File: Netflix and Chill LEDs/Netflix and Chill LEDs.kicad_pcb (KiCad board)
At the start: 2 copper layers, 17.8 x 48.3 mm, 0 parts

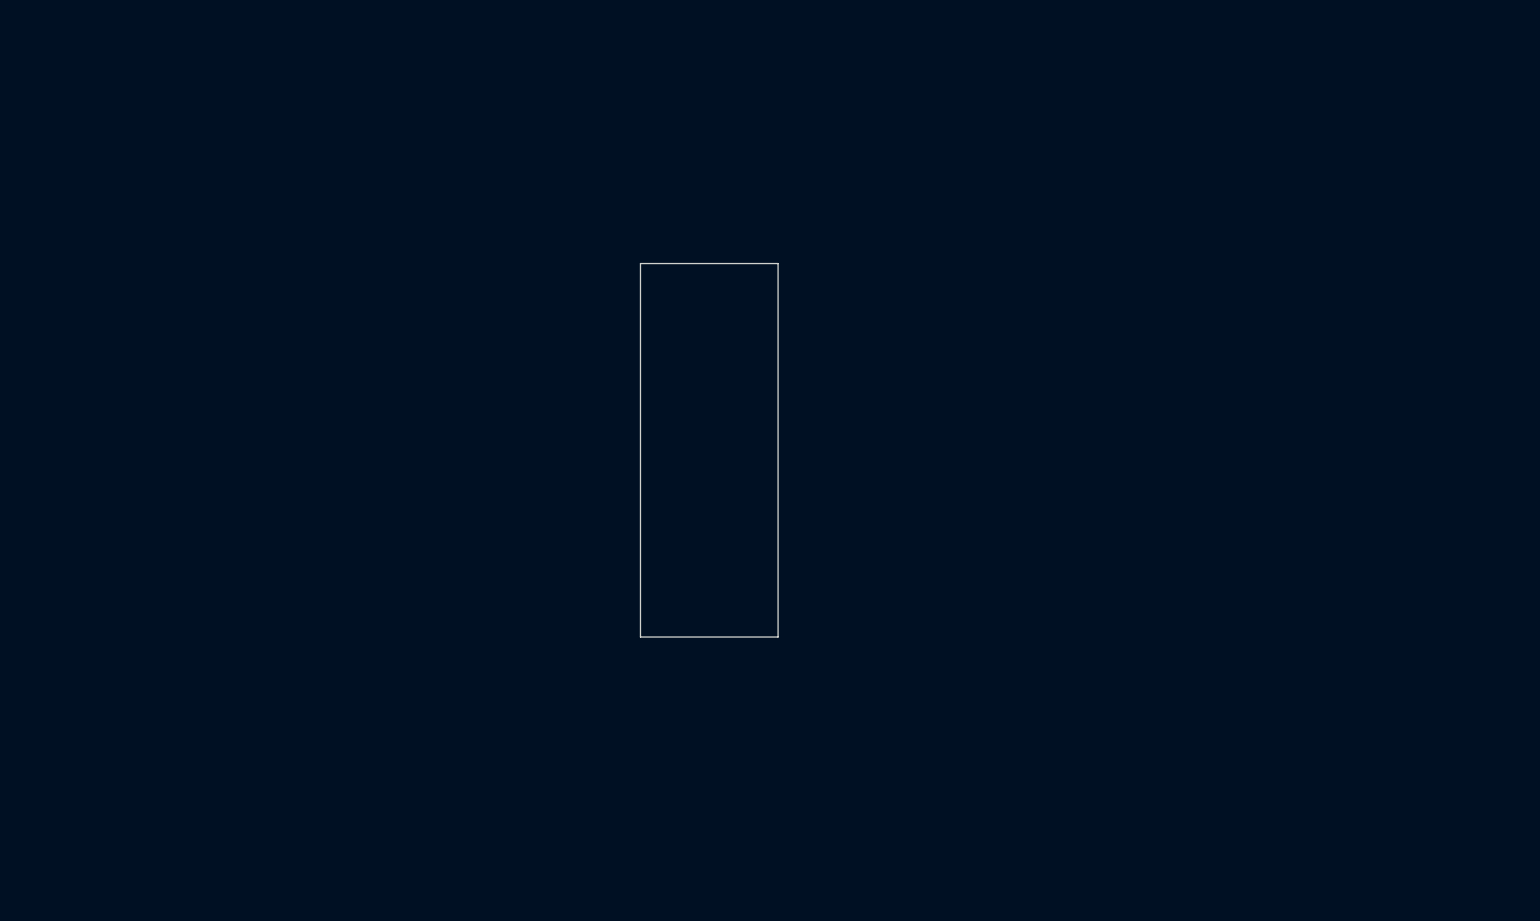
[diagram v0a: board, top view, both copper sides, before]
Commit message: board base design done
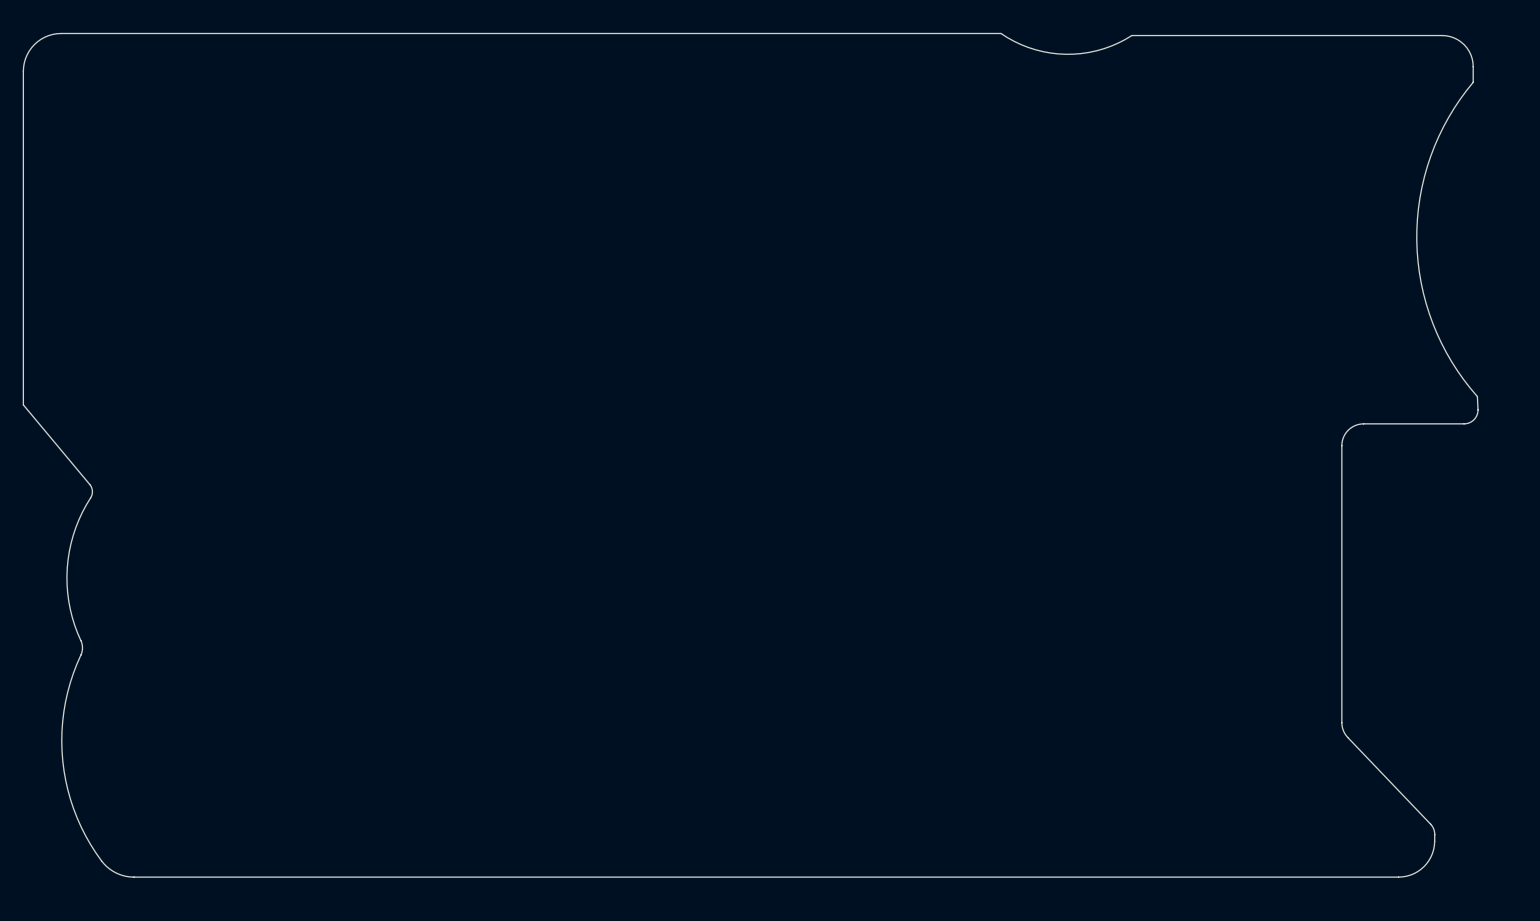
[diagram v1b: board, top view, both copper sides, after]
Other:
- board size 17.8 x 48.3 mm -> 188 x 109 mm

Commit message: placement and routing done
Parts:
- added C1: 1uF, Capacitor_SMD:C_0603_1608Metric, F.Cu at (62.0, 38.8)
- added C10: 1uF, Capacitor_SMD:C_0603_1608Metric, F.Cu at (206.8, 38.8)
- added C11: 1uF, Capacitor_SMD:C_0603_1608Metric, F.Cu at (223.0, 38.8)
- added C12: 1uF, Capacitor_SMD:C_0603_1608Metric, F.Cu at (238.8, 38.8)
- added C13: 1uF, Capacitor_SMD:C_0603_1608Metric, F.Cu at (60.5, 58.8)
- added C14: 1uF, Capacitor_SMD:C_0603_1608Metric, F.Cu at (78.0, 58.8)
- added C15: 1uF, Capacitor_SMD:C_0603_1608Metric, F.Cu at (94.5, 58.8)
- added C16: 1uF, Capacitor_SMD:C_0603_1608Metric, F.Cu at (105.2, 58.8)
- added C17: 1uF, Capacitor_SMD:C_0603_1608Metric, F.Cu at (129.0, 58.8)
- added C18: 1uF, Capacitor_SMD:C_0603_1608Metric, F.Cu at (151.8, 58.8)
- added C19: 1uF, Capacitor_SMD:C_0603_1608Metric, F.Cu at (162.0, 58.8)
- added C2: 1uF, Capacitor_SMD:C_0603_1608Metric, F.Cu at (78.0, 38.8)
- added C20: 1uF, Capacitor_SMD:C_0603_1608Metric, F.Cu at (179.5, 58.8)
- added C21: 1uF, Capacitor_SMD:C_0603_1608Metric, F.Cu at (206.8, 58.8)
- added C22: 1uF, Capacitor_SMD:C_0603_1608Metric, F.Cu at (231.0, 58.8)
- added C23: 1uF, Capacitor_SMD:C_0603_1608Metric, F.Cu at (60.5, 80.2)
- added C24: 1uF, Capacitor_SMD:C_0603_1608Metric, F.Cu at (77.0, 80.2)
- added C25: 1uF, Capacitor_SMD:C_0603_1608Metric, F.Cu at (94.5, 80.2)
- added C26: 1uF, Capacitor_SMD:C_0603_1608Metric, F.Cu at (107.0, 80.2)
- added C27: 1uF, Capacitor_SMD:C_0603_1608Metric, F.Cu at (129.0, 80.2)
- added C28: 1uF, Capacitor_SMD:C_0603_1608Metric, F.Cu at (151.8, 80.2)
- added C29: 1uF, Capacitor_SMD:C_0603_1608Metric, F.Cu at (179.5, 80.2)
- added C3: 1uF, Capacitor_SMD:C_0603_1608Metric, F.Cu at (94.5, 38.8)
- added C30: 1uF, Capacitor_SMD:C_0603_1608Metric, F.Cu at (192.0, 80.2)
- added C31: 1uF, Capacitor_SMD:C_0603_1608Metric, F.Cu at (206.8, 80.2)
- added C32: 1uF, Capacitor_SMD:C_0603_1608Metric, F.Cu at (222.5, 80.2)
- added C33: 1uF, Capacitor_SMD:C_0603_1608Metric, F.Cu at (238.8, 80.2)
- added C34: 1uF, Capacitor_SMD:C_0603_1608Metric, F.Cu at (79.8, 96.2)
- added C35: 1uF, Capacitor_SMD:C_0603_1608Metric, F.Cu at (117.8, 96.2)
- added C36: 1uF, Capacitor_SMD:C_0603_1608Metric, F.Cu at (144.8, 96.2)
- added C37: 1uF, Capacitor_SMD:C_0603_1608Metric, F.Cu at (160.2, 96.2)
- added C38: 1uF, Capacitor_SMD:C_0603_1608Metric, F.Cu at (177.2, 96.2)
- added C39: 1uF, Capacitor_SMD:C_0603_1608Metric, F.Cu at (194.0, 96.2)
- added C4: 1uF, Capacitor_SMD:C_0603_1608Metric, F.Cu at (107.0, 38.8)
- added C40: 1uF, Capacitor_SMD:C_0603_1608Metric, F.Cu at (221.8, 96.2)
- added C41: 1uF, Capacitor_SMD:C_0603_1608Metric, F.Cu at (67.2, 103.0)
- added C42: 1uF, Capacitor_SMD:C_0603_1608Metric, F.Cu at (129.2, 104.8)
- added C43: 1uF, Capacitor_SMD:C_0603_1608Metric, F.Cu at (71.5, 115.8)
- added C44: 1uF, Capacitor_SMD:C_0603_1608Metric, F.Cu at (82.8, 115.8)
- added C45: 1uF, Capacitor_SMD:C_0603_1608Metric, F.Cu at (114.2, 115.8)
- added C46: 1uF, Capacitor_SMD:C_0603_1608Metric, F.Cu at (144.8, 115.8)
- added C47: 1uF, Capacitor_SMD:C_0603_1608Metric, F.Cu at (160.2, 115.8)
- added C48: 1uF, Capacitor_SMD:C_0603_1608Metric, F.Cu at (177.2, 115.8)
- added C49: 1uF, Capacitor_SMD:C_0603_1608Metric, F.Cu at (194.0, 115.8)
- added C5: 1uF, Capacitor_SMD:C_0603_1608Metric, F.Cu at (121.0, 38.8)
- added C50: 1uF, Capacitor_SMD:C_0603_1608Metric, F.Cu at (221.8, 115.8)
- added C51: 1uF, Capacitor_SMD:C_0603_1608Metric, F.Cu at (129.2, 127.2)
- added C52: 1uF, Capacitor_SMD:C_0603_1608Metric, F.Cu at (67.2, 131.8)
- added C53: 1uF, Capacitor_SMD:C_0603_1608Metric, F.Cu at (82.2, 137.8)
- added C54: 1uF, Capacitor_SMD:C_0603_1608Metric, F.Cu at (117.2, 137.8)
- added C55: 1uF, Capacitor_SMD:C_0603_1608Metric, F.Cu at (144.8, 137.8)
- added C56: 1uF, Capacitor_SMD:C_0603_1608Metric, F.Cu at (160.2, 137.8)
- added C57: 1uF, Capacitor_SMD:C_0603_1608Metric, F.Cu at (177.2, 137.8)
- added C58: 1uF, Capacitor_SMD:C_0603_1608Metric, F.Cu at (194.0, 137.8)
- added C59: 1uF, Capacitor_SMD:C_0603_1608Metric, F.Cu at (207.0, 137.8)
- added C6: 1uF, Capacitor_SMD:C_0603_1608Metric, F.Cu at (137.2, 38.8)
- added C60: 1uF, Capacitor_SMD:C_0603_1608Metric, F.Cu at (221.8, 137.8)
- added C61: 1uF, Capacitor_SMD:C_0603_1608Metric, F.Cu at (234.0, 137.8)
- added C7: 1uF, Capacitor_SMD:C_0603_1608Metric, F.Cu at (151.8, 38.8)
- added C8: 1uF, Capacitor_SMD:C_0603_1608Metric, F.Cu at (164.5, 38.8)
- added C9: 1uF, Capacitor_SMD:C_0603_1608Metric, F.Cu at (179.5, 38.8)
- added D1: WS2812B, LED_SMD:LED_WS2812B_PLCC4_5.0x5.0mm_P3.2mm, F.Cu at (62.0, 42.5)
- added D10: WS2812B, LED_SMD:LED_WS2812B_PLCC4_5.0x5.0mm_P3.2mm, F.Cu at (206.8, 42.5)
- added D11: WS2812B, LED_SMD:LED_WS2812B_PLCC4_5.0x5.0mm_P3.2mm, F.Cu at (223.0, 42.5)
- added D12: WS2812B, LED_SMD:LED_WS2812B_PLCC4_5.0x5.0mm_P3.2mm, F.Cu at (238.8, 42.5)
- added D13: WS2812B, LED_SMD:LED_WS2812B_PLCC4_5.0x5.0mm_P3.2mm, F.Cu at (60.5, 62.5)
- added D14: WS2812B, LED_SMD:LED_WS2812B_PLCC4_5.0x5.0mm_P3.2mm, F.Cu at (78.0, 62.5)
- added D15: WS2812B, LED_SMD:LED_WS2812B_PLCC4_5.0x5.0mm_P3.2mm, F.Cu at (94.5, 62.5)
- added D16: WS2812B, LED_SMD:LED_WS2812B_PLCC4_5.0x5.0mm_P3.2mm, F.Cu at (105.2, 62.5)
- added D17: WS2812B, LED_SMD:LED_WS2812B_PLCC4_5.0x5.0mm_P3.2mm, F.Cu at (129.0, 62.5)
- added D18: WS2812B, LED_SMD:LED_WS2812B_PLCC4_5.0x5.0mm_P3.2mm, F.Cu at (151.8, 62.5)
- added D19: WS2812B, LED_SMD:LED_WS2812B_PLCC4_5.0x5.0mm_P3.2mm, F.Cu at (162.0, 62.5)
- added D2: WS2812B, LED_SMD:LED_WS2812B_PLCC4_5.0x5.0mm_P3.2mm, F.Cu at (78.0, 42.5)
- added D20: WS2812B, LED_SMD:LED_WS2812B_PLCC4_5.0x5.0mm_P3.2mm, F.Cu at (179.5, 62.5)
- added D21: WS2812B, LED_SMD:LED_WS2812B_PLCC4_5.0x5.0mm_P3.2mm, F.Cu at (206.8, 62.5)
- added D22: WS2812B, LED_SMD:LED_WS2812B_PLCC4_5.0x5.0mm_P3.2mm, F.Cu at (231.0, 62.5)
- added D23: WS2812B, LED_SMD:LED_WS2812B_PLCC4_5.0x5.0mm_P3.2mm, F.Cu at (60.5, 84.0)
- added D24: WS2812B, LED_SMD:LED_WS2812B_PLCC4_5.0x5.0mm_P3.2mm, F.Cu at (77.0, 84.0)
- added D25: WS2812B, LED_SMD:LED_WS2812B_PLCC4_5.0x5.0mm_P3.2mm, F.Cu at (94.5, 84.0)
- added D26: WS2812B, LED_SMD:LED_WS2812B_PLCC4_5.0x5.0mm_P3.2mm, F.Cu at (107.0, 84.0)
- added D27: WS2812B, LED_SMD:LED_WS2812B_PLCC4_5.0x5.0mm_P3.2mm, F.Cu at (129.0, 84.0)
- added D28: WS2812B, LED_SMD:LED_WS2812B_PLCC4_5.0x5.0mm_P3.2mm, F.Cu at (151.8, 84.0)
- added D29: WS2812B, LED_SMD:LED_WS2812B_PLCC4_5.0x5.0mm_P3.2mm, F.Cu at (179.5, 84.0)
- added D3: WS2812B, LED_SMD:LED_WS2812B_PLCC4_5.0x5.0mm_P3.2mm, F.Cu at (94.5, 42.5)
- added D30: WS2812B, LED_SMD:LED_WS2812B_PLCC4_5.0x5.0mm_P3.2mm, F.Cu at (192.0, 84.0)
- added D31: WS2812B, LED_SMD:LED_WS2812B_PLCC4_5.0x5.0mm_P3.2mm, F.Cu at (206.8, 84.0)
- added D32: WS2812B, LED_SMD:LED_WS2812B_PLCC4_5.0x5.0mm_P3.2mm, F.Cu at (222.5, 84.0)
- added D33: WS2812B, LED_SMD:LED_WS2812B_PLCC4_5.0x5.0mm_P3.2mm, F.Cu at (238.8, 84.0)
- added D34: WS2812B, LED_SMD:LED_WS2812B_PLCC4_5.0x5.0mm_P3.2mm, F.Cu at (79.8, 100.0)
- added D35: WS2812B, LED_SMD:LED_WS2812B_PLCC4_5.0x5.0mm_P3.2mm, F.Cu at (117.8, 100.0)
- added D36: WS2812B, LED_SMD:LED_WS2812B_PLCC4_5.0x5.0mm_P3.2mm, F.Cu at (144.8, 100.0)
- added D37: WS2812B, LED_SMD:LED_WS2812B_PLCC4_5.0x5.0mm_P3.2mm, F.Cu at (160.2, 100.0)
- added D38: WS2812B, LED_SMD:LED_WS2812B_PLCC4_5.0x5.0mm_P3.2mm, F.Cu at (177.2, 100.0)
- added D39: WS2812B, LED_SMD:LED_WS2812B_PLCC4_5.0x5.0mm_P3.2mm, F.Cu at (194.0, 100.0)
- added D4: WS2812B, LED_SMD:LED_WS2812B_PLCC4_5.0x5.0mm_P3.2mm, F.Cu at (107.0, 42.5)
- added D40: WS2812B, LED_SMD:LED_WS2812B_PLCC4_5.0x5.0mm_P3.2mm, F.Cu at (221.8, 100.0)
- added D41: WS2812B, LED_SMD:LED_WS2812B_PLCC4_5.0x5.0mm_P3.2mm, F.Cu at (67.2, 106.8)
- added D42: WS2812B, LED_SMD:LED_WS2812B_PLCC4_5.0x5.0mm_P3.2mm, F.Cu at (129.2, 108.5)
- added D43: WS2812B, LED_SMD:LED_WS2812B_PLCC4_5.0x5.0mm_P3.2mm, F.Cu at (71.5, 119.5)
- added D44: WS2812B, LED_SMD:LED_WS2812B_PLCC4_5.0x5.0mm_P3.2mm, F.Cu at (82.8, 119.5)
- added D45: WS2812B, LED_SMD:LED_WS2812B_PLCC4_5.0x5.0mm_P3.2mm, F.Cu at (114.2, 119.5)
- added D46: WS2812B, LED_SMD:LED_WS2812B_PLCC4_5.0x5.0mm_P3.2mm, F.Cu at (144.8, 119.5)
- added D47: WS2812B, LED_SMD:LED_WS2812B_PLCC4_5.0x5.0mm_P3.2mm, F.Cu at (160.2, 119.5)
- added D48: WS2812B, LED_SMD:LED_WS2812B_PLCC4_5.0x5.0mm_P3.2mm, F.Cu at (177.2, 119.5)
- added D49: WS2812B, LED_SMD:LED_WS2812B_PLCC4_5.0x5.0mm_P3.2mm, F.Cu at (194.0, 119.5)
- added D5: WS2812B, LED_SMD:LED_WS2812B_PLCC4_5.0x5.0mm_P3.2mm, F.Cu at (121.0, 42.5)
- added D50: WS2812B, LED_SMD:LED_WS2812B_PLCC4_5.0x5.0mm_P3.2mm, F.Cu at (221.8, 119.5)
- added D51: WS2812B, LED_SMD:LED_WS2812B_PLCC4_5.0x5.0mm_P3.2mm, F.Cu at (129.2, 131.0)
- added D52: WS2812B, LED_SMD:LED_WS2812B_PLCC4_5.0x5.0mm_P3.2mm, F.Cu at (67.2, 135.5)
- added D53: WS2812B, LED_SMD:LED_WS2812B_PLCC4_5.0x5.0mm_P3.2mm, F.Cu at (82.2, 141.5)
- added D54: WS2812B, LED_SMD:LED_WS2812B_PLCC4_5.0x5.0mm_P3.2mm, F.Cu at (117.2, 141.5)
- added D55: WS2812B, LED_SMD:LED_WS2812B_PLCC4_5.0x5.0mm_P3.2mm, F.Cu at (144.8, 141.5)
- added D56: WS2812B, LED_SMD:LED_WS2812B_PLCC4_5.0x5.0mm_P3.2mm, F.Cu at (160.2, 141.5)
- added D57: WS2812B, LED_SMD:LED_WS2812B_PLCC4_5.0x5.0mm_P3.2mm, F.Cu at (177.2, 141.5)
- added D58: WS2812B, LED_SMD:LED_WS2812B_PLCC4_5.0x5.0mm_P3.2mm, F.Cu at (194.0, 141.5)
- added D59: WS2812B, LED_SMD:LED_WS2812B_PLCC4_5.0x5.0mm_P3.2mm, F.Cu at (207.0, 141.5)
- added D6: WS2812B, LED_SMD:LED_WS2812B_PLCC4_5.0x5.0mm_P3.2mm, F.Cu at (137.2, 42.5)
- added D60: WS2812B, LED_SMD:LED_WS2812B_PLCC4_5.0x5.0mm_P3.2mm, F.Cu at (221.8, 141.5)
- added D61: WS2812B, LED_SMD:LED_WS2812B_PLCC4_5.0x5.0mm_P3.2mm, F.Cu at (234.0, 141.5)
- added D7: WS2812B, LED_SMD:LED_WS2812B_PLCC4_5.0x5.0mm_P3.2mm, F.Cu at (151.8, 42.5)
- added D8: WS2812B, LED_SMD:LED_WS2812B_PLCC4_5.0x5.0mm_P3.2mm, F.Cu at (164.5, 42.5)
- added D9: WS2812B, LED_SMD:LED_WS2812B_PLCC4_5.0x5.0mm_P3.2mm, F.Cu at (179.5, 42.5)
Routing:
- net +5V: track 0.00 -> 1328.7 mm
- net Net-(D22-Pad2): track 0.00 -> 189.0 mm
- net Net-(D33-Pad2): track 0.00 -> 177.7 mm
- net GND: track 0.00 -> 172.8 mm, vias 0 -> 122
- net Net-(D40-Pad2): track 0.00 -> 153.4 mm
- net Net-(D50-Pad2): track 0.00 -> 91.0 mm
- net Net-(D42-Pad2): track 0.00 -> 71.6 mm
- net Net-(D41-Pad2): track 0.00 -> 69.1 mm
- net Net-(D51-Pad2): track 0.00 -> 57.6 mm
- net Net-(D34-Pad2): track 0.00 -> 44.2 mm
- net Net-(D53-Pad2): track 0.00 -> 41.2 mm
- net Net-(D44-Pad2): track 0.00 -> 37.7 mm
- net Net-(D45-Pad2): track 0.00 -> 36.7 mm
- net Net-(D39-Pad2): track 0.00 -> 34.0 mm
- net Net-(D49-Pad2): track 0.00 -> 34.0 mm
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- added copper zone on B.Cu, net GND

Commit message: layout done
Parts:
- added J2: CONN_02, Connector_PinHeader_2.54mm:PinHeader_1x02_P2.54mm_Vertical, B.Cu at (218.1, 133.3)
- added U1: PixelBlazePico, _Breadstick_Footprints:PixelBlazePico, B.Cu at (101.2, 48.4)
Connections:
- D1 pad 4: unconnected-(D1-Pad4) -> Net-(D1-Pad4)
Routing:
- net Net-(D12-Pad2): track 0.00 -> 180.7 mm
- net Net-(D1-Pad4): track 0.00 -> 41.2 mm, vias 0 -> 1
- net Net-(D22-Pad2): track 189.0 -> 173.2 mm
- net +5V: track 1328.7 -> 1336.8 mm, vias 0 -> 19
- added copper zone on B.Cu, net +5V
- added copper zone on In1.Cu, net GND
- added copper zone on In2.Cu, net GND
- removed copper zone on B.Cu, net GND
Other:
- copper layers 2 -> 4
